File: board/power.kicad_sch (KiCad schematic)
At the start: 18 parts, among them J11 Conn_01x03_Male, J12 Conn_01x02_Male, J13 Conn_01x02_Male, J14 Conn_01x03_Male, U4 LD3985M33R_SOT23

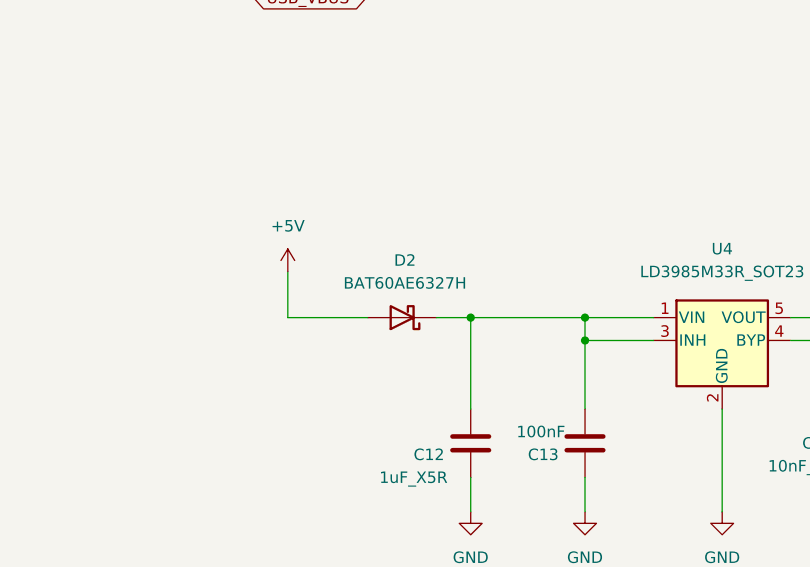
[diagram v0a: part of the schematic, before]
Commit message: created firmware project. Tested MIDI communication over MIDI port as well as USB MIDI
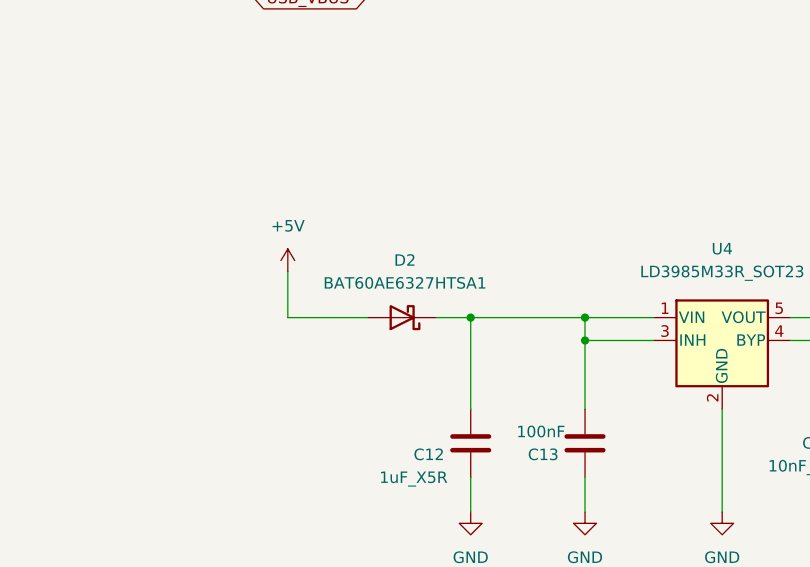
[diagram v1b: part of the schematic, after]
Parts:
- C10, C12, C15: Digi-Key Part Number (none) -> 1276-2396-1-ND
- C11: Digi-Key Part Number (none) -> 1276-6455-1-ND
- C13, C6, C7, C8, C9: Digi-Key Part Number (none) -> 1276-1003-1-ND
- C14, C4, C5: Digi-Key Part Number (none) -> 1276-1015-1-ND
- D2: value BAT60AE6327H -> BAT60AE6327HTSA1; Digi-Key Part Number (none) -> BAT60AE6327HTSA1CT-ND; LCSC C520634 -> (none); Manufacturer_Part_Number BAT60AE6327H -> BAT60AE6327HTSA1
- J11, J14: Digi-Key Part Number (none) -> HTSW-103-14-TM-S-ND
- J12, J13: Digi-Key Part Number (none) -> HTSW-102-14-TM-S-ND
- U4: Digi-Key Part Number (none) -> 497-3504-1-ND
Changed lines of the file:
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@@
+      (effects (font (size 1.27 1.27)) hide)
+    )
+    (property "Digi-Key Part Number" "1276-6455-1-ND" (id 9) (at 146.05 153.67 0)
       (effects (font (size 1.27 1.27)) hide)
     )
@@
       (effects (font (size 1.27 1.27)) hide)
     )
+    (property "Digi-Key Part Number" "HTSW-103-14-TM-S-ND" (id 8) (at 69.85 41.91 0)
+      (effects (font (size 1.27 1.27)) hide)
+    )
     (pin "1")
     (pin "2")
@@
       (effects (font (size 1.27 1.27)) hide)
     )
+    (property "Digi-Key Part Number" "1276-2396-1-ND" (id 9) (at 217.17 92.71 0)
+      (effects (font (size 1.27 1.27)) hide)
+    )
     (pin "1")
     (pin "2")
@@
       (effects (font (size 1.27 1.27)) hide)
     )
+    (property "Digi-Key Part Number" "HTSW-102-14-TM-S-ND" (id 8) (at 74.93 68.58 0)
+      (effects (font (size 1.27 1.27)) hide)
+    )
     (pin "1")
     (pin "2")
@@
     )
     (property "LCSC" "C1710" (id 8) (at 68.58 153.67 0)
+      (effects (font (size 1.27 1.27)) hide)
+    )
+    (property "Digi-Key Part Number" "1276-1015-1-ND" (id 9) (at 68.58 153.67 0)
       (effects (font (size 1.27 1.27)) hide)
     )
@@
     )
     (property "LCSC" "C1711" (id 8) (at 91.44 153.67 0)
+      (effects (font (size 1.27 1.27)) hide)
+    )
+    (property "Digi-Key Part Number" "1276-1003-1-ND" (id 9) (at 91.44 153.67 0)
       (effects (font (size 1.27 1.27)) hide)
     )
@@
       (effects (font (size 1.27 1.27)) hide)
     )
+    (property "Digi-Key Part Number" "497-3504-1-ND" (id 9) (at 187.96 82.55 0)
+      (effects (font (size 1.27 1.27)) hide)
+    )
     (pin "1")
     (pin "2")
@@
       (effects (font (size 1.27 1.27)) hide)
     )
+    (property "Digi-Key Part Number" "HTSW-103-14-TM-S-ND" (id 8) (at 129.54 41.91 0)
+      (effects (font (size 1.27 1.27)) hide)
+    )
     (pin "1")
     (pin "2")
@@
     )
     (property "LCSC" "C1711" (id 8) (at 102.87 153.67 0)
+      (effects (font (size 1.27 1.27)) hide)
+    )
+    (property "Digi-Key Part Number" "1276-1003-1-ND" (id 9) (at 102.87 153.67 0)
       (effects (font (size 1.27 1.27)) hide)
     )
@@
       (effects (font (size 1.27 1.27)) hide)
     )
+    (property "Digi-Key Part Number" "HTSW-102-14-TM-S-ND" (id 8) (at 74.93 96.52 0)
+      (effects (font (size 1.27 1.27)) hide)
+    )
     (pin "1")
     (pin "2")
@@
     )
     (property "LCSC" "C318694" (id 8) (at 135.89 153.67 0)
+      (effects (font (size 1.27 1.27)) hide)
+    )
+    (property "Digi-Key Part Number" "1276-2396-1-ND" (id 9) (at 135.89 153.67 0)
       (effects (font (size 1.27 1.27)) hide)
     )
@@
       (effects (font (size 1.27 1.27)) hide)
     )
+    (property "Digi-Key Part Number" "1276-1015-1-ND" (id 9) (at 203.2 92.71 0)
+      (effects (font (size 1.27 1.27)) hide)
+    )
     (pin "1")
     (pin "2")
@@
       (effects (font (size 1.27 1.27)) hide)
     )
+    (property "Digi-Key Part Number" "1276-1015-1-ND" (id 9) (at 80.01 153.67 0)
+      (effects (font (size 1.27 1.27)) hide)
+    )
     (pin "1")
     (pin "2")
@@
     (in_bom yes) (on_board yes) (fields_autoplaced)
     (property "Reference" "D2" (id 0) (at 152.7175 73.66 0))
-    (property "Value" "BAT60AE6327H" (id 1) (at 152.7175 76.2 0))
+    (property "Value" "BAT60AE6327HTSA1" (id 1) (at 152.7175 76.2 0))
     (property "Footprint" "Diode_SMD:D_SOD-323" (id 2) (at 152.4 75.565 0)
       (effects (font (size 1.27 1.27)) hide)
     )
-    (property "Datasheet" "https://datasheet.lcsc.com/lcsc/2005091632_Infineon-Technologies-BAT60AE6327H_C520634.pdf" (id 3) (at 152.4 80.01 0)
+    (property "Datasheet" "https://www.infineon.com/dgdl/bat60aseries.pdf?folderId=db3a304313d846880113def5812204a1&fileId=db3a304313d846880113def70c9304a9" (id 3) (at 152.4 80.01 0)
       (effects (font (size 1.27 1.27)) hide)
     )
@@
       (effects (font (size 1.27 1.27)) hide)
     )
-    (property "Manufacturer_Part_Number" "BAT60AE6327H" (id 7) (at 152.4 80.01 0)
-      (effects (font (size 1.27 1.27)) hide)
-    )
-    (property "LCSC" "C520634" (id 8) (at 152.4 80.01 0)
+    (property "Manufacturer_Part_Number" "BAT60AE6327HTSA1" (id 7) (at 152.4 80.01 0)
+      (effects (font (size 1.27 1.27)) hide)
+    )
+    (property "LCSC" "" (id 8) (at 152.4 80.01 0)
+      (effects (font (size 1.27 1.27)) hide)
+    )
+    (property "Digi-Key Part Number" "BAT60AE6327HTSA1CT-ND" (id 9) (at 152.4 80.01 0)
       (effects (font (size 1.27 1.27)) hide)
     )
@@
       (effects (font (size 1.27 1.27)) hide)
     )
+    (property "Digi-Key Part Number" "1276-1003-1-ND" (id 9) (at 124.46 153.67 0)
+      (effects (font (size 1.27 1.27)) hide)
+    )
     (pin "1")
     (pin "2")
@@
       (effects (font (size 1.27 1.27)) hide)
     )
+    (property "Digi-Key Part Number" "1276-1003-1-ND" (id 9) (at 114.3 153.67 0)
+      (effects (font (size 1.27 1.27)) hide)
+    )
     (pin "1")
     (pin "2")
@@
     )
     (property "LCSC" "C1711" (id 8) (at 172.72 93.98 0)
+      (effects (font (size 1.27 1.27)) hide)
+    )
+    (property "Digi-Key Part Number" "1276-1003-1-ND" (id 9) (at 172.72 93.98 0)
       (effects (font (size 1.27 1.27)) hide)
     )
@@
       (effects (font (size 1.27 1.27)) hide)
     )
+    (property "Digi-Key Part Number" "1276-2396-1-ND" (id 9) (at 160.02 93.98 0)
+      (effects (font (size 1.27 1.27)) hide)
+    )
